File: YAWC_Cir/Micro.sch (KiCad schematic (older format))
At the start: 11 parts, among them P3 CONN_5, P4 CONN_5, P5 CONN_6, U2 SAMD20J18A-M

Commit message: Stuff
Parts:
- added J_Midi1, J_Rst1: CONN_2, symbol CONN_2
- added R4: R, symbol R
- added SER1: CONN_3X2, symbol CONN_3X2
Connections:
- net labels added: S1P0, S1P1, S1P2, S1P3, SCL, SDA, Tx
- wire segments 29 -> 54
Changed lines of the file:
@@
 LIBS:opto
 LIBS:atmel
+LIBS:MySymbols
+LIBS:MyComponents
 LIBS:contrib
 LIBS:valves
@@
 	1    0    0    -1
 $EndComp
-Wire Wire Line
-	5400 5050 5400 5250
-Wire Wire Line
-	5400 5250 5950 5250
-Wire Wire Line
-	5700 5050 5700 5350
-Wire Wire Line
-	5500 5050 5500 5250
-Connection ~ 5500 5250
-Wire Wire Line
-	5600 5050 5600 5250
-Connection ~ 5600 5250
-Connection ~ 5700 5250
-Wire Wire Line
-	5950 5250 5950 5050
 Text GLabel 5400 1100 1    60   Input ~ 0
 VCC
-Wire Wire Line
-	5100 1550 5100 1200
-Wire Wire Line
-	5100 1200 5950 1200
-Wire Wire Line
-	5400 1200 5400 1100
-Connection ~ 5300 1200
-Wire Wire Line
-	5500 1200 5500 1550
-Connection ~ 5400 1200
-Wire Wire Line
-	5600 1200 5600 1550
-Connection ~ 5500 1200
-Wire Wire Line
-	5700 1200 5700 1550
-Connection ~ 5600 1200
-Wire Wire Line
-	5950 1200 5950 1550
-Connection ~ 5700 1200
 Text GLabel 1500 1150 1    60   Input ~ 0
 VCC
@@
 	1    0    0    -1
 $EndComp
-Wire Wire Line
-	1150 1250 1900 1250
-Connection ~ 1650 1250
-Wire Wire Line
-	1150 1650 1900 1650
-Connection ~ 1400 1650
-Connection ~ 1650 1650
-Wire Wire Line
-	1500 1750 1500 1650
-Connection ~ 1500 1650
-Wire Wire Line
-	1500 1150 1500 1250
-Connection ~ 1500 1250
 $Comp
 L C C7
@@
 	1    0    0    -1
 $EndComp
-Wire Wire Line
-	4100 1350 4100 1300
-Wire Wire Line
-	4100 1300 4350 1300
-Wire Wire Line
-	4750 1300 5300 1300
-Wire Wire Line
-	5300 1300 5300 1550
 Text Label 7550 2050 0    60   ~ 0
 Y0
@@
 	1    0    0    -1
 $EndComp
-Wire Wire Line
-	9700 1050 9700 1150
-Wire Wire Line
-	9700 1650 9700 1800
-Connection ~ 9700 1800
 Text Label 10000 1800 1    60   ~ 0
 Reset
-Wire Wire Line
-	9700 1800 10000 1800
 Text Label 7550 4650 0    60   ~ 0
 SWCLK
@@
 	1    0    0    -1
 $EndComp
-Wire Wire Line
-	9700 2350 9700 2200
-Wire Wire Line
-	9700 2200 10000 2200
-Wire Wire Line
-	10000 2100 9500 2100
-Wire Wire Line
-	9500 2100 9500 1150
-Wire Wire Line
-	9500 1150 9700 1150
 Text GLabel 9700 2200 0    60   Input ~ 0
 GND
@@
 Text GLabel 9400 2950 2    60   Input ~ 0
 Bth
+$Comp
+L CONN_2 J_Rst1
+U 1 1 539AD121
+P 10450 2850
+F 0 "J_Rst1" V 10400 2850 40  0000 C CNN
+F 1 "CONN_2" V 10500 2850 40  0000 C CNN
+F 2 "" H 10450 2850 60  0000 C CNN
+F 3 "" H 10450 2850 60  0000 C CNN
+	1    10450 2850
+	1    0    0    -1
+$EndComp
+$Comp
+L GND #PWR07
+U 1 1 539AD16E
+P 10050 3100
+F 0 "#PWR07" H 10050 3100 30  0001 C CNN
+F 1 "GND" H 10050 3030 30  0001 C CNN
+F 2 "" H 10050 3100 60  0000 C CNN
+F 3 "" H 10050 3100 60  0000 C CNN
+	1    10050 3100
+	1    0    0    -1
+$EndComp
+Text Label 10100 2750 2    60   ~ 0
+Reset
+$Comp
+L CONN_3X2 SER1
+U 1 1 539AD3BB
+P 10100 3750
+F 0 "SER1" H 10100 4000 50  0000 C CNN
+F 1 "CONN_3X2" V 10100 3800 40  0000 C CNN
+F 2 "" H 10100 3750 60  0000 C CNN
+F 3 "" H 10100 3750 60  0000 C CNN
+	1    10100 3750
+	0    -1   -1   0
+$EndComp
+Wire Wire Line
+	5400 5050 5400 5250
+Wire Wire Line
+	5400 5250 5950 5250
+Wire Wire Line
+	5700 5050 5700 5350
+Wire Wire Line
+	5500 5050 5500 5250
+Connection ~ 5500 5250
+Wire Wire Line
+	5600 5050 5600 5250
+Connection ~ 5600 5250
+Connection ~ 5700 5250
+Wire Wire Line
+	5950 5250 5950 5050
+Wire Wire Line
+	5100 1550 5100 1200
+Wire Wire Line
+	5100 1200 5950 1200
+Wire Wire Line
+	5400 1200 5400 1100
+Connection ~ 5300 1200
+Wire Wire Line
+	5500 1200 5500 1550
+Connection ~ 5400 1200
+Wire Wire Line
+	5600 1200 5600 1550
+Connection ~ 5500 1200
+Wire Wire Line
+	5700 1200 5700 1550
+Connection ~ 5600 1200
+Wire Wire Line
+	5950 1200 5950 1550
+Connection ~ 5700 1200
+Wire Wire Line
+	1150 1250 1900 1250
+Connection ~ 1650 1250
+Wire Wire Line
+	1150 1650 1900 1650
+Connection ~ 1400 1650
+Connection ~ 1650 1650
+Wire Wire Line
+	1500 1750 1500 1650
+Connection ~ 1500 1650
+Wire Wire Line
+	1500 1150 1500 1250
+Connection ~ 1500 1250
+Wire Wire Line
+	4100 1350 4100 1300
+Wire Wire Line
+	4100 1300 4350 1300
+Wire Wire Line
+	4750 1300 5300 1300
+Wire Wire Line
+	5300 1300 5300 1550
+Wire Wire Line
+	9700 1050 9700 1150
+Wire Wire Line
+	9700 1650 9700 1800
+Connection ~ 9700 1800
+Wire Wire Line
+	9700 1800 10000 1800
+Wire Wire Line
+	9700 2350 9700 2200
+Wire Wire Line
+	9700 2200 10000 2200
+Wire Wire Line
+	10000 2100 9500 2100
+Wire Wire Line
+	9500 2100 9500 1150
+Wire Wire Line
+	9500 1150 9700 1150
+Wire Wire Line
+	10100 2950 10050 2950
+Wire Wire Line
+	10050 2950 10050 3100
+Wire Wire Line
+	7550 3450 9250 3450
+Wire Wire Line
+	9250 3450 9250 4150
+Wire Wire Line
+	9250 4150 9950 4150
+Wire Wire Line
+	7550 3550 9700 3550
+Wire Wire Line
+	9700 3550 9700 3350
+Wire Wire Line
+	9700 3350 9950 3350
+Wire Wire Line
+	7550 3650 9150 3650
+Wire Wire Line
+	9150 3650 9150 4200
+Wire Wire Line
+	9150 4200 10050 4200
+Wire Wire Line
+	10050 4200 10050 4150
+Wire Wire Line
+	7550 3750 9650 3750
+Wire Wire Line
+	9650 3750 9650 3300
+Wire Wire Line
+	9650 3300 10050 3300
+Wire Wire Line
+	10050 3300 10050 3350
+Text Label 10150 3350 0    60   ~ 0
+VCC
+$Comp
+L GND #PWR08
+U 1 1 539AD64C
+P 10150 4150
+F 0 "#PWR08" H 10150 4150 30  0001 C CNN
+F 1 "GND" H 10150 4080 30  0001 C CNN
+F 2 "" H 10150 4150 60  0000 C CNN
+F 3 "" H 10150 4150 60  0000 C CNN
+	1    10150 4150
+	1    0    0    -1
+$EndComp
+Text Label 9250 3450 0    60   ~ 0
+S1P0
+Text Label 9350 3550 0    60   ~ 0
+S1P1
+Text Label 9150 4050 2    60   ~ 0
+S1P2
+Text Label 9350 3750 0    60   ~ 0
+S1P3
+Wire Wire Line
+	7550 3050 7800 3050
+Text Label 7800 3050 0    60   ~ 0
+Tx
+$Comp
+L CONN_2 J_Midi1
+U 1 1 539ADB47
+P 10500 4750
+F 0 "J_Midi1" V 10450 4750 40  0000 C CNN
+F 1 "CONN_2" V 10550 4750 40  0000 C CNN
+F 2 "" H 10500 4750 60  0000 C CNN
+F 3 "" H 10500 4750 60  0000 C CNN
+	1    10500 4750
+	1    0    0    -1
+$EndComp
+$Comp
+L R R4
+U 1 1 539ADC21
+P 9700 4650
+F 0 "R4" V 9780 4650 40  0000 C CNN
+F 1 "R" V 9707 4651 40  0000 C CNN
+F 2 "" V 9630 4650 30  0000 C CNN
+F 3 "" H 9700 4650 30  0000 C CNN
+	1    9700 4650
+	0    1    1    0
+$EndComp
+Wire Wire Line
+	9950 4650 10150 4650
+Wire Wire Line
+	9450 4650 9250 4650
+Text Label 9250 4650 2    60   ~ 0
+Tx
+$Comp
+L GND #PWR09
+U 1 1 539ADD4F
+P 10100 4950
+F 0 "#PWR09" H 10100 4950 30  0001 C CNN
+F 1 "GND" H 10100 4880 30  0001 C CNN
+F 2 "" H 10100 4950 60  0000 C CNN
+F 3 "" H 10100 4950 60  0000 C CNN
+	1    10100 4950
+	1    0    0    -1
+$EndComp
+Wire Wire Line
+	10150 4850 10100 4850
+Wire Wire Line
+	10100 4850 10100 4950
+Text GLabel 8150 1200 1    60   Input ~ 0
+SDA
+Text GLabel 8450 1200 1    60   Input ~ 0
+SCL
+Wire Wire Line
+	7550 4050 8150 4050
+Wire Wire Line
+	8150 4050 8150 1200
+Wire Wire Line
+	8450 1200 8450 4150
+Wire Wire Line
+	8450 4150 7550 4150
 $EndSCHEMATC

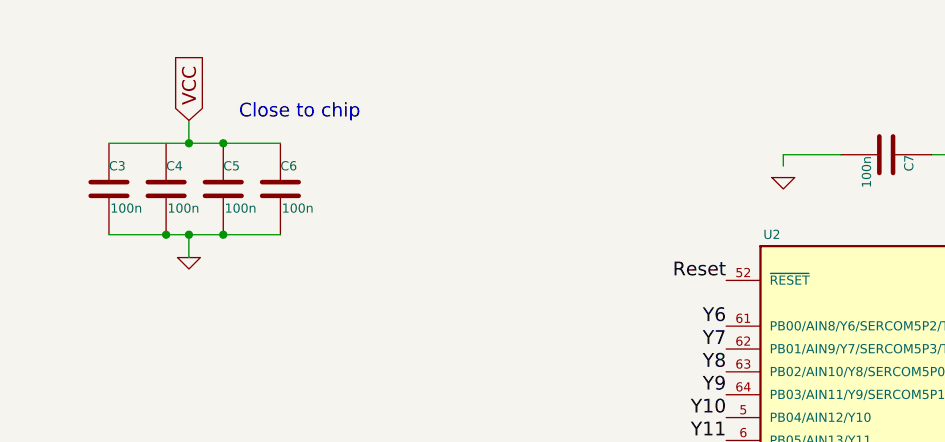
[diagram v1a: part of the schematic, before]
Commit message: Update pad sizes
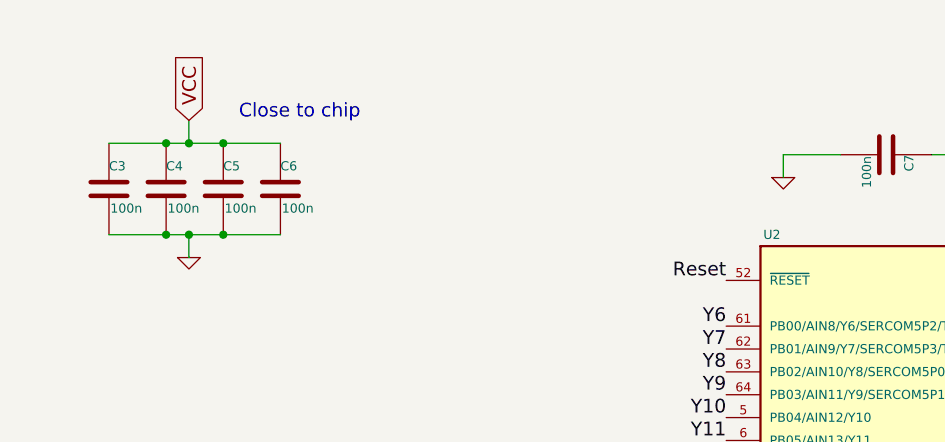
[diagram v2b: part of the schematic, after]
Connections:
- net GND: now also C7.2
- net VCC: now also C4.1
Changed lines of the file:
@@
 Connection ~ 1500 1250
 Wire Wire Line
-	4100 1350 4100 1300
+	4100 1300 4100 1400
 Wire Wire Line
 	4100 1300 4350 1300
@@
 Wire Wire Line
 	8450 4150 7550 4150
+Connection ~ 1400 1250
 $EndSCHEMATC

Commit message: Buttons. Need to DRC
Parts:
- added P2: Btns, symbol CONN_3X2
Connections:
- net GND: now also P2.1, P2.5
- net Y11: now also P3.4; no longer P4.1
- net Y12: now also P3.3; no longer P3.4
- net Y13: now also P3.2; no longer P4.2
- net Y14: now also P3.1; no longer P3.3
- net Y15: now also P4.1; no longer P4.3
- net Y2: now also P4.2; no longer P3.2
- net Y3: now also P4.3; no longer P4.4
- net Y4: now also P4.4; no longer P3.1
- net PB11: now reaches U2.24 (PB11/SERCOM4P3/TC5WO1/GCLKIO5)
- net PB11: now also P2.3
- net PB12: now reaches U2.25 (PB12/X12/SERC0M4P0/TC4WO0/GCLKIO6)
- net PB12: now also P2.2
- net PB13: now reaches U2.26 (PB13/X13/SERCOM4P1/TC4WO1/GCLKIO7)
- net PB13: now also P2.4
- net PB14: now reaches U2.27 (PB14/X14/SERCOM4P2/TC5WO0/GCLKIO0)
- net PB14: now also P2.6
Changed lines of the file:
@@
 Pin headers.
 Text Label 1700 4150 0    60   ~ 0
+Y14
+Text Label 1700 5050 0    60   ~ 0
+Y15
+Text Label 1700 4250 0    60   ~ 0
+Y13
+Text Label 1700 5150 0    60   ~ 0
+Y2
+Text Label 1700 4350 0    60   ~ 0
+Y12
+Text Label 1700 5250 0    60   ~ 0
+Y3
+Text Label 1700 4450 0    60   ~ 0
+Y11
+Text Label 1700 5350 0    60   ~ 0
 Y4
-Text Label 1700 5050 0    60   ~ 0
-Y11
-Text Label 1700 4250 0    60   ~ 0
-Y2
-Text Label 1700 5150 0    60   ~ 0
-Y13
-Text Label 1700 4350 0    60   ~ 0
-Y14
-Text Label 1700 5250 0    60   ~ 0
-Y15
-Text Label 1700 4450 0    60   ~ 0
-Y12
-Text Label 1700 5350 0    60   ~ 0
-Y3
 Text Label 1700 4550 0    60   ~ 0
 Y10
@@
 	8450 4150 7550 4150
 Connection ~ 1400 1250
+$Comp
+L CONN_3X2 P2
+U 1 1 539DD48F
+P 1550 2700
+F 0 "P2" H 1550 2950 50  0000 C CNN
+F 1 "Btns" V 1550 2750 40  0000 C CNN
+F 2 "" H 1550 2700 60  0000 C CNN
+F 3 "" H 1550 2700 60  0000 C CNN
+	1    1550 2700
+	1    0    0    -1
+$EndComp
+$Comp
+L GND #PWR010
+U 1 1 539DD52C
+P 900 2900
+F 0 "#PWR010" H 900 2900 30  0001 C CNN
+F 1 "GND" H 900 2830 30  0001 C CNN
+F 2 "" H 900 2900 60  0000 C CNN
+F 3 "" H 900 2900 60  0000 C CNN
+	1    900  2900
+	1    0    0    -1
+$EndComp
+Wire Wire Line
+	900  2900 900  2550
+Wire Wire Line
+	900  2550 1150 2550
+Wire Wire Line
+	1150 2750 900  2750
+Connection ~ 900  2750
+Text Label 1150 2650 2    60   ~ 0
+PB11
+Text Label 1950 2550 0    60   ~ 0
+PB12
+Text Label 1950 2650 0    60   ~ 0
+PB13
+Text Label 1950 2750 0    60   ~ 0
+PB14
+Text Label 3850 3150 2    60   ~ 0
+PB11
+Text Label 3850 3250 2    60   ~ 0
+PB12
+Text Label 3850 3350 2    60   ~ 0
+PB13
+Text Label 3850 3450 2    60   ~ 0
+PB14
 $EndSCHEMATC

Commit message: More updates. Foot prints still to check
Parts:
- added ATP1, ATP2: CONN_1, symbol CONN_1
- added D1: LED, symbol LED
- added R5: 350, symbol R
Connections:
- net PB11: now also P2.2; no longer P2.3
- net PB12: now also P2.3; no longer P2.2
- net VCC: now also R5.2
- net at U2.17 (TC0WO0/SERCOM2P0/SERCOM0P0/X0/AIN16/NMI/PA08): now also ATP1.1
- net at U2.18 (TC0WO1/SERCOM2P1/SERCOM0P1/X1/AIN17/PA09): now also ATP2.1
- net at U2.59 (PB30/SERC0M5P0/TC0WO0): now also D1.2 (K)
- new net: D1.1 (A), R5.1
- no-connect marks 0 -> 18
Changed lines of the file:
@@
-	1    0    0    -1
-$EndComp
-$Comp
-L GND #PWR03
-U 1 1 5394B7FB
-P 5700 5350
-F 0 "#PWR03" H 5700 5350 30  0001 C CNN
-F 1 "GND" H 5700 5280 30  0001 C CNN
-F 2 "" H 5700 5350 60  0000 C CNN
-F 3 "" H 5700 5350 60  0000 C CNN
-	1    5700 5350
 	1    0    0    -1
 $EndComp
@@
 Text GLabel 1500 1150 1    60   Input ~ 0
 VCC
-$Comp
-L GND #PWR04
-U 1 1 5397365F
-P 1500 1750
-F 0 "#PWR04" H 1500 1750 30  0001 C CNN
-F 1 "GND" H 1500 1680 30  0001 C CNN
-F 2 "" H 1500 1750 60  0000 C CNN
-F 3 "" H 1500 1750 60  0000 C CNN
-	1    1500 1750
-	1    0    0    -1
-$EndComp
 $Comp
 L C C3
@@
 $EndComp
 $Comp
-L GND #PWR05
+L GND #PWR04
 U 1 1 539738BC
 P 4100 1400
-F 0 "#PWR05" H 4100 1400 30  0001 C CNN
+F 0 "#PWR04" H 4100 1400 30  0001 C CNN
 F 1 "GND" H 4100 1330 30  0001 C CNN
 F 2 "" H 4100 1400 60  0000 C CNN
@@
 SWCLK
 $Comp
-L GND #PWR06
+L GND #PWR05
 U 1 1 5398A8C9
 P 9700 2350
-F 0 "#PWR06" H 9700 2350 30  0001 C CNN
+F 0 "#PWR05" H 9700 2350 30  0001 C CNN
 F 1 "GND" H 9700 2280 30  0001 C CNN
 F 2 "" H 9700 2350 60  0000 C CNN
@@
 	1    0    0    -1
 $EndComp
-$Comp
-L GND #PWR07
-U 1 1 539AD16E
-P 10050 3100
-F 0 "#PWR07" H 10050 3100 30  0001 C CNN
-F 1 "GND" H 10050 3030 30  0001 C CNN
-F 2 "" H 10050 3100 60  0000 C CNN
-F 3 "" H 10050 3100 60  0000 C CNN
-	1    10050 3100
-	1    0    0    -1
-$EndComp
 Text Label 10100 2750 2    60   ~ 0
 Reset
@@
 	5400 5050 5400 5250
 Wire Wire Line
-	5400 5250 5950 5250
-Wire Wire Line
-	5700 5050 5700 5350
-Wire Wire Line
-	5500 5050 5500 5250
-Connection ~ 5500 5250
-Wire Wire Line
-	5600 5050 5600 5250
-Connection ~ 5600 5250
-Connection ~ 5700 5250
-Wire Wire Line
-	5950 5250 5950 5050
-Wire Wire Line
 	5100 1550 5100 1200
 Wire Wire Line
@@
 Connection ~ 1650 1250
 Wire Wire Line
-	1150 1650 1900 1650
+	950  1650 1900 1650
 Connection ~ 1400 1650
 Connection ~ 1650 1650
 Wire Wire Line
-	1500 1750 1500 1650
+	1500 1650 1500 1850
 Connection ~ 1500 1650
 Wire Wire Line
@@
 Wire Wire Line
 	9500 1150 9700 1150
-Wire Wire Line
-	10100 2950 10050 2950
-Wire Wire Line
-	10050 2950 10050 3100
 Wire Wire Line
 	7550 3450 9250 3450
@@
 VCC
 $Comp
-L GND #PWR08
+L GND #PWR06
 U 1 1 539AD64C
 P 10150 4150
-F 0 "#PWR08" H 10150 4150 30  0001 C CNN
+F 0 "#PWR06" H 10150 4150 30  0001 C CNN
 F 1 "GND" H 10150 4080 30  0001 C CNN
 F 2 "" H 10150 4150 60  0000 C CNN
@@
 Text Label 9250 4650 2    60   ~ 0
 Tx
-$Comp
-L GND #PWR09
-U 1 1 539ADD4F
-P 10100 4950
-F 0 "#PWR09" H 10100 4950 30  0001 C CNN
-F 1 "GND" H 10100 4880 30  0001 C CNN
-F 2 "" H 10100 4950 60  0000 C CNN
-F 3 "" H 10100 4950 60  0000 C CNN
-	1    10100 4950
-	1    0    0    -1
-$EndComp
-Wire Wire Line
-	10150 4850 10100 4850
-Wire Wire Line
-	10100 4850 10100 4950
+Wire Wire Line
+	10000 4850 10150 4850
 Text GLabel 8150 1200 1    60   Input ~ 0
 SDA
@@
 	1    0    0    -1
 $EndComp
-$Comp
-L GND #PWR010
-U 1 1 539DD52C
-P 900 2900
-F 0 "#PWR010" H 900 2900 30  0001 C CNN
-F 1 "GND" H 900 2830 30  0001 C CNN
-F 2 "" H 900 2900 60  0000 C CNN
-F 3 "" H 900 2900 60  0000 C CNN
-	1    900  2900
-	1    0    0    -1
-$EndComp
-Wire Wire Line
-	900  2900 900  2550
-Wire Wire Line
-	900  2550 1150 2550
-Wire Wire Line
-	1150 2750 900  2750
-Connection ~ 900  2750
 Text Label 1150 2650 2    60   ~ 0
+PB12
+Text Label 1950 2550 0    60   ~ 0
 PB11
-Text Label 1950 2550 0    60   ~ 0
-PB12
 Text Label 1950 2650 0    60   ~ 0
 PB13
@@
 Text Label 3850 3450 2    60   ~ 0
 PB14
+$Comp
+L CONN_1 ATP1
+U 1 1 539ECD18
+P 7850 2650
+F 0 "ATP1" H 7930 2650 40  0000 L CNN
+F 1 "CONN_1" H 7850 2705 30  0001 C CNN
+F 2 "" H 7850 2650 60  0000 C CNN
+F 3 "" H 7850 2650 60  0000 C CNN
+	1    7850 2650
+	1    0    0    -1
+$EndComp
+$Comp
+L CONN_1 ATP2
+U 1 1 539ECD77
+P 7850 2750
+F 0 "ATP2" H 7930 2750 40  0000 L CNN
+F 1 "CONN_1" H 7850 2805 30  0001 C CNN
+F 2 "" H 7850 2750 60  0000 C CNN
+F 3 "" H 7850 2750 60  0000 C CNN
+	1    7850 2750
+	1    0    0    -1
+$EndComp
+Wire Wire Line
+	7550 2650 7700 2650
+Wire Wire Line
+	7700 2750 7550 2750
+$Comp
+L LED D1
+U 1 1 539ED0A8
+P 3350 4050
+F 0 "D1" H 3350 4150 50  0000 C CNN
+F 1 "LED" H 3350 3950 50  0000 C CNN
+F 2 "" H 3350 4050 60  0000 C CNN
+F 3 "" H 3350 4050 60  0000 C CNN
+	1    3350 4050
+	1    0    0    -1
+$EndComp
+Wire Wire Line
+	3550 4050 3850 4050
+$Comp
+L R R5
+U 1 1 539ED159
+P 2750 4050
+F 0 "R5" V 2830 4050 40  0000 C CNN
+F 1 "350" V 2757 4051 40  0000 C CNN
+F 2 "" V 2680 4050 30  0000 C CNN
+F 3 "" H 2750 4050 30  0000 C CNN
+	1    2750 4050
+	0    1    1    0
+$EndComp
+Text Label 2500 4050 2    60   ~ 0
+VCC
+Wire Wire Line
+	3000 4050 3150 4050
+NoConn ~ 3850 3050
+NoConn ~ 3850 3550
+NoConn ~ 3850 3650
+NoConn ~ 3850 3750
+NoConn ~ 3850 3850
+NoConn ~ 3850 3950
+NoConn ~ 3850 4150
+NoConn ~ 7550 4250
+NoConn ~ 7550 4350
+NoConn ~ 7550 4450
+NoConn ~ 7550 4550
+NoConn ~ 7550 3950
+NoConn ~ 7550 3850
+NoConn ~ 7550 3350
+NoConn ~ 7550 3250
+NoConn ~ 7550 3150
+NoConn ~ 7550 1850
+NoConn ~ 7550 1950
+Wire Wire Line
+	9950 2950 10100 2950
+Wire Wire Line
+	5400 5250 5950 5250
+Wire Wire Line
+	5950 5250 5950 5050
+Wire Wire Line
+	10000 4850 10000 5050
+Wire Wire Line
+	950  2750 1150 2750
+$Comp
+L GND #PWR07
+U 1 1 539EEC3B
+P 9950 3000
+F 0 "#PWR07" H 9950 3000 30  0001 C CNN
+F 1 "GND" H 9950 2930 30  0001 C CNN
+F 2 "" H 9950 3000 60  0000 C CNN
+F 3 "" H 9950 3000 60  0000 C CNN
+	1    9950 3000
+	1    0    0    -1
+$EndComp
+Wire Wire Line
+	9950 3000 9950 2950
+Wire Wire Line
+	1150 2550 950  2550
+Connection ~ 950  2750
+$Comp
+L GND #PWR08
+U 1 1 539EF45E
+P 5700 5400
+F 0 "#PWR08" H 5700 5400 30  0001 C CNN
+F 1 "GND" H 5700 5330 30  0001 C CNN
+F 2 "" H 5700 5400 60  0000 C CNN
+F 3 "" H 5700 5400 60  0000 C CNN
+	1    5700 5400
+	1    0    0    -1
+$EndComp
+Text GLabel 1750 1900 3    60   Input ~ 0
+GND
+Wire Wire Line
+	1750 1900 1750 1650
+Connection ~ 1750 1650
+$Comp
+L GND #PWR09
+U 1 1 539EF936
+P 1500 1850
+F 0 "#PWR09" H 1500 1850 30  0001 C CNN
+F 1 "GND" H 1500 1780 30  0001 C CNN
+F 2 "" H 1500 1850 60  0000 C CNN
+F 3 "" H 1500 1850 60  0000 C CNN
+	1    1500 1850
+	1    0    0    -1
+$EndComp
+$Comp
+L GND #PWR010
+U 1 1 539EFA2D
+P 10000 5050
+F 0 "#PWR010" H 10000 5050 30  0001 C CNN
+F 1 "GND" H 10000 4980 30  0001 C CNN
+F 2 "" H 10000 5050 60  0000 C CNN
+F 3 "" H 10000 5050 60  0000 C CNN
+	1    10000 5050
+	1    0    0    -1
+$EndComp
+Connection ~ 1150 1650
+Connection ~ 950  2550
+Text Label 10000 4850 2    60   ~ 0
+GND
+Text Label 5400 5250 2    60   ~ 0
+GND
+Wire Wire Line
+	5500 5050 5500 5250
+Connection ~ 5500 5250
+Wire Wire Line
+	5600 5050 5600 5250
+Connection ~ 5600 5250
+Connection ~ 5700 5250
+Wire Wire Line
+	950  1650 950  2750
+Wire Wire Line
+	5700 5050 5700 5400
 $EndSCHEMATC

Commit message: Route not finished. Components done
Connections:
- net PB12: now also P2.4; no longer P2.3
- net PB13: now also P2.6; no longer P2.4
- net PB14: now also P2.3; no longer P2.6
- net Y0: now also P5.5; no longer P5.1
- net Y1: now also P5.6; no longer P5.2
- net Y6: now also P5.1; no longer P5.6
- net Y7: now also P5.2; no longer P5.5
- net Y8: now also P5.3; no longer P5.4
- net Y9: now also P5.4; no longer P5.3
- net BatSample: now reaches ATP2.1, U2.18 (TC0WO1/SERCOM2P1/SERCOM0P1/X1/AIN17/PA09)
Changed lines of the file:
@@
 Y5
 Text Label 1650 6000 0    60   ~ 0
+Y6
+Text Label 1650 6100 0    60   ~ 0
+Y7
+Text Label 1650 6200 0    60   ~ 0
+Y8
+Text Label 1650 6300 0    60   ~ 0
+Y9
+Text Label 1650 6400 0    60   ~ 0
 Y0
-Text Label 1650 6100 0    60   ~ 0
+Text Label 1650 6500 0    60   ~ 0
 Y1
-Text Label 1650 6200 0    60   ~ 0
-Y9
-Text Label 1650 6300 0    60   ~ 0
-Y8
-Text Label 1650 6400 0    60   ~ 0
-Y7
-Text Label 1650 6500 0    60   ~ 0
-Y6
 Text Label 3850 1850 2    60   ~ 0
 Reset
@@
 $EndComp
 Text Label 1150 2650 2    60   ~ 0
-PB12
+PB14
 Text Label 1950 2550 0    60   ~ 0
 PB11
 Text Label 1950 2650 0    60   ~ 0
+PB12
+Text Label 1950 2750 0    60   ~ 0
 PB13
-Text Label 1950 2750 0    60   ~ 0
-PB14
 Text Label 3850 3150 2    60   ~ 0
 PB11
@@
 Wire Wire Line
 	5700 5050 5700 5400
+Wire Wire Line
+	7700 2750 7700 2850
+Wire Wire Line
+	7700 2850 7850 2850
+Text GLabel 7850 2850 2    60   Input ~ 0
+BatSample
 $EndSCHEMATC

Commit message: All routed and DRC No gnd fill No silk screen detail done
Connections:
- net S1P0: now also SER1.4; no longer SER1.1
- net S1P1: now also SER1.3; no longer SER1.2
- net S1P2: now also SER1.2; no longer SER1.3
- net S1P3: now also SER1.1; no longer SER1.4
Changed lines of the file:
@@
 	7550 3450 9250 3450
 Wire Wire Line
-	9250 3450 9250 4150
-Wire Wire Line
-	9250 4150 9950 4150
-Wire Wire Line
 	7550 3550 9700 3550
 Wire Wire Line
-	9700 3550 9700 3350
-Wire Wire Line
-	9700 3350 9950 3350
-Wire Wire Line
-	7550 3650 9150 3650
-Wire Wire Line
-	9150 3650 9150 4200
-Wire Wire Line
-	9150 4200 10050 4200
+	7550 3650 9800 3650
 Wire Wire Line
 	10050 4200 10050 4150
@@
 	7550 3750 9650 3750
 Wire Wire Line
-	9650 3750 9650 3300
-Wire Wire Line
-	9650 3300 10050 3300
-Wire Wire Line
-	10050 3300 10050 3350
+	10050 3200 10050 3350
 Text Label 10150 3350 0    60   ~ 0
 VCC
@@
 Text Label 9350 3550 0    60   ~ 0
 S1P1
-Text Label 9150 4050 2    60   ~ 0
+Text Label 9950 3350 2    60   ~ 0
 S1P2
 Text Label 9350 3750 0    60   ~ 0
@@
 Text GLabel 7850 2850 2    60   Input ~ 0
 BatSample
+Wire Wire Line
+	9650 3750 9650 4150
+Connection ~ 9650 4150
+Wire Wire Line
+	9650 4150 9950 4150
+Wire Wire Line
+	9250 3200 10050 3200
+Connection ~ 9250 3450
+Wire Wire Line
+	9250 3450 9250 3200
+Wire Wire Line
+	9700 3550 9700 4200
+Connection ~ 9700 4200
+Wire Wire Line
+	9700 4200 10050 4200
+Wire Wire Line
+	9800 3650 9800 3350
+Wire Wire Line
+	9800 3350 9950 3350
+Connection ~ 9150 3650
 $EndSCHEMATC
